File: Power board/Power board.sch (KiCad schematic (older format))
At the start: 6 parts

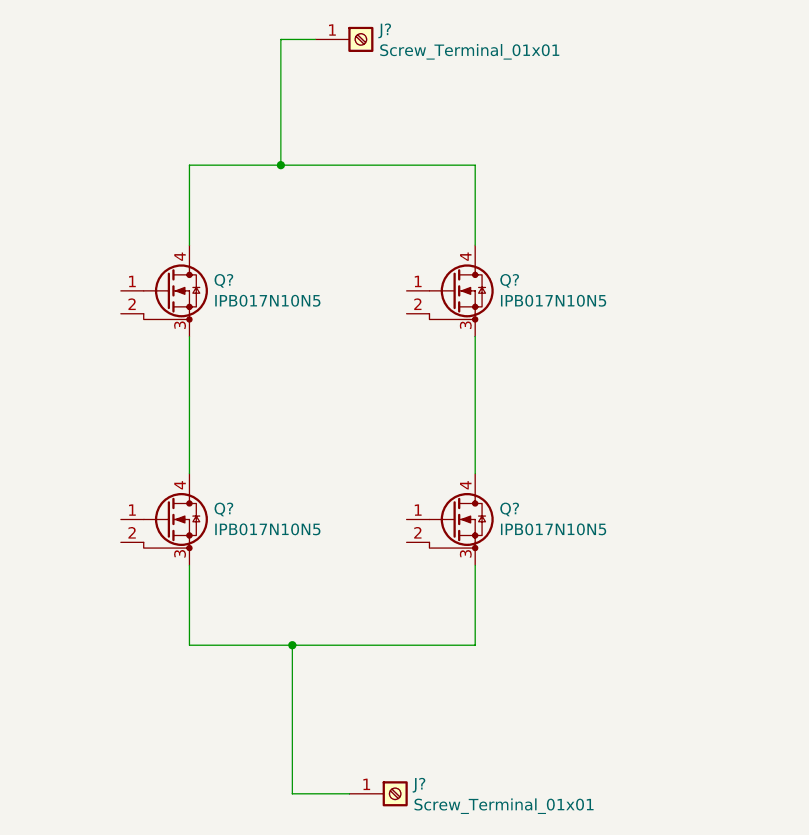
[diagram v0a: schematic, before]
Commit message: Gate resistors is added to power board
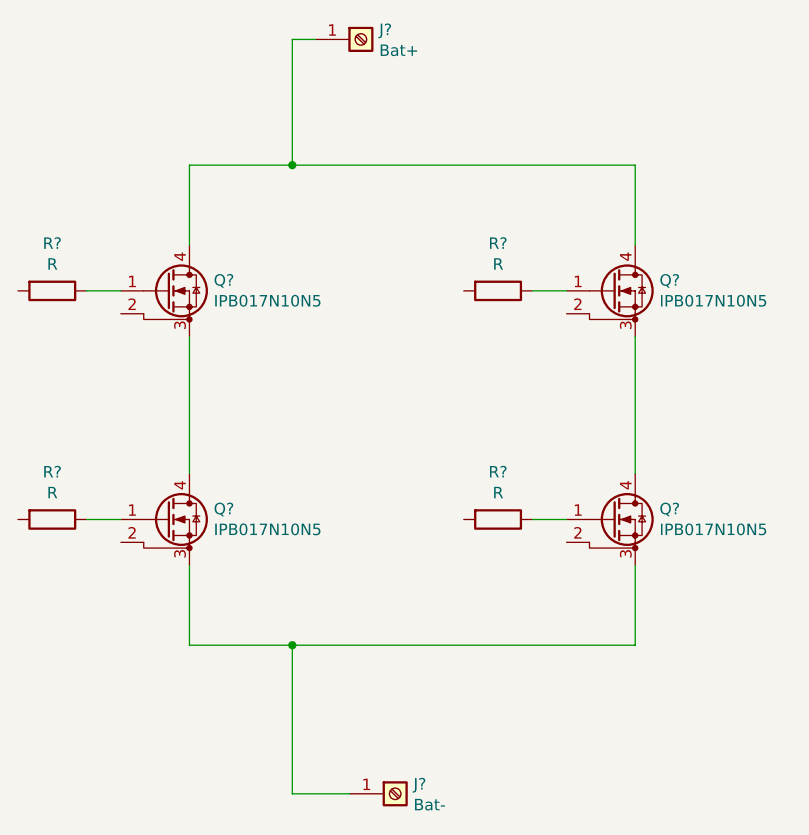
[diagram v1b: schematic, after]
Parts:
- added R? (x4): R, symbol Device:R
- J?: value Screw_Terminal_01x01 -> Bat+
- J?: value Screw_Terminal_01x01 -> Bat-
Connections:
- net at Q?.1 (G): now also R?.1 (x4)
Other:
- moved on the sheet: Q?
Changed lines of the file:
@@
 EESchema Schematic File Version 4
+LIBS:Power board-cache
 EELAYER 29 0
 EELAYER END
@@
 L Vikings_actives:IPB017N10N5 Q?
 U 1 1 5CB8FD8E
-P 5650 2250
-F 0 "Q?" H 5856 2296 50  0000 L CNN
-F 1 "IPB017N10N5" H 5856 2205 50  0000 L CNN
-F 2 "Package_TO_SOT_SMD:TO-263-7_TabPin8" H 5650 2250 50  0001 C CIN
-F 3 "https://www.wolfspeed.com/media/downloads/145/C3M0065090J.pdf" H 5650 2250 50  0001 L CNN
-	1    5650 2250
+P 6350 2250
+F 0 "Q?" H 6556 2296 50  0000 L CNN
+F 1 "IPB017N10N5" H 6556 2205 50  0000 L CNN
+F 2 "Package_TO_SOT_SMD:TO-263-7_TabPin8" H 6350 2250 50  0001 C CIN
+F 3 "https://www.wolfspeed.com/media/downloads/145/C3M0065090J.pdf" H 6350 2250 50  0001 L CNN
+	1    6350 2250
 	1    0    0    -1
 $EndComp
@@
 L Vikings_actives:IPB017N10N5 Q?
 U 1 1 5CB94E76
-P 5650 3250
-F 0 "Q?" H 5856 3296 50  0000 L CNN
-F 1 "IPB017N10N5" H 5856 3205 50  0000 L CNN
-F 2 "Package_TO_SOT_SMD:TO-263-7_TabPin8" H 5650 3250 50  0001 C CIN
-F 3 "https://www.wolfspeed.com/media/downloads/145/C3M0065090J.pdf" H 5650 3250 50  0001 L CNN
-	1    5650 3250
+P 6350 3250
+F 0 "Q?" H 6556 3296 50  0000 L CNN
+F 1 "IPB017N10N5" H 6556 3205 50  0000 L CNN
+F 2 "Package_TO_SOT_SMD:TO-263-7_TabPin8" H 6350 3250 50  0001 C CIN
+F 3 "https://www.wolfspeed.com/media/downloads/145/C3M0065090J.pdf" H 6350 3250 50  0001 L CNN
+	1    6350 3250
 	1    0    0    -1
 $EndComp
@@
 P 5250 1150
 F 0 "J?" H 5330 1192 50  0000 L CNN
-F 1 "Screw_Terminal_01x01" H 5330 1101 50  0000 L CNN
+F 1 "Bat+" H 5330 1101 50  0000 L CNN
 F 2 "" H 5250 1150 50  0001 C CNN
 F 3 "~" H 5250 1150 50  0001 C CNN
@@
 $EndComp
 Wire Wire Line
-	5050 1150 4900 1150
-Wire Wire Line
-	4900 1150 4900 1700
-Wire Wire Line
-	4900 1700 4500 1700
-Wire Wire Line
 	4500 1700 4500 2050
 Wire Wire Line
-	4900 1700 5750 1700
-Wire Wire Line
-	5750 1700 5750 2050
-Connection ~ 4900 1700
+	6450 1700 6450 2050
 Wire Wire Line
 	4500 2450 4500 3050
 Wire Wire Line
-	5750 2450 5750 3050
+	6450 2450 6450 3050
 Wire Wire Line
-	5750 3450 5750 3800
-Wire Wire Line
-	5750 3800 4950 3800
+	6450 3450 6450 3800
 Wire Wire Line
 	4500 3800 4500 3450
@@
 P 5400 4450
 F 0 "J?" H 5480 4492 50  0000 L CNN
-F 1 "Screw_Terminal_01x01" H 5480 4401 50  0000 L CNN
+F 1 "Bat-" H 5480 4401 50  0000 L CNN
 F 2 "" H 5400 4450 50  0001 C CNN
 F 3 "~" H 5400 4450 50  0001 C CNN
@@
 Wire Wire Line
 	4950 4450 4950 3800
-Connection ~ 4950 3800
 Wire Wire Line
 	4950 3800 4500 3800
+$Comp
+L Device:R R?
+U 1 1 5CC099DA
+P 3900 2250
+F 0 "R?" V 3693 2250 50  0000 C CNN
+F 1 "R" V 3784 2250 50  0000 C CNN
+F 2 "" V 3830 2250 50  0001 C CNN
+F 3 "~" H 3900 2250 50  0001 C CNN
+	1    3900 2250
+	0    1    1    0
+$EndComp
+$Comp
+L Device:R R?
+U 1 1 5CC0B578
+P 3900 3250
+F 0 "R?" V 3693 3250 50  0000 C CNN
+F 1 "R" V 3784 3250 50  0000 C CNN
+F 2 "" V 3830 3250 50  0001 C CNN
+F 3 "~" H 3900 3250 50  0001 C CNN
+	1    3900 3250
+	0    1    1    0
+$EndComp
+$Comp
+L Device:R R?
+U 1 1 5CC0C047
+P 5850 3250
+F 0 "R?" V 5643 3250 50  0000 C CNN
+F 1 "R" V 5734 3250 50  0000 C CNN
+F 2 "" V 5780 3250 50  0001 C CNN
+F 3 "~" H 5850 3250 50  0001 C CNN
+	1    5850 3250
+	0    1    1    0
+$EndComp
+Wire Wire Line
+	4950 3800 6450 3800
+Connection ~ 4950 3800
+$Comp
+L Device:R R?
+U 1 1 5CC100FA
+P 5850 2250
+F 0 "R?" V 5643 2250 50  0000 C CNN
+F 1 "R" V 5734 2250 50  0000 C CNN
+F 2 "" V 5780 2250 50  0001 C CNN
+F 3 "~" H 5850 2250 50  0001 C CNN
+	1    5850 2250
+	0    1    1    0
+$EndComp
+Wire Wire Line
+	4500 1700 4950 1700
+Wire Wire Line
+	4950 1700 4950 1150
+Wire Wire Line
+	4950 1150 5050 1150
+Connection ~ 4950 1700
+Wire Wire Line
+	4950 1700 6450 1700
+Wire Wire Line
+	6150 2250 6000 2250
+Wire Wire Line
+	4200 2250 4050 2250
+Wire Wire Line
+	6150 3250 6000 3250
+Wire Wire Line
+	4200 3250 4050 3250
 $EndSCHEMATC

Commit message: schematic is done
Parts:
- removed J?: Bat+, symbol Connector:Screw_Terminal_01x01
- removed J?: Bat-, symbol Connector:Screw_Terminal_01x01
- added C1, C2: 0.033u, Capacitors_SMD:C_0805, symbol Device:C
- added C3: 1u, Capacitors_SMD:C_0805, symbol Device:C
- added J1: High1, Pin_Headers:Pin_Header_Straight_1x02_Pitch2.54mm_SMD_Pin1Left, symbol Connector_Generic:Conn_01x02
- added J2: Low1, Pin_Headers:Pin_Header_Straight_1x02_Pitch2.54mm_SMD_Pin1Left, symbol Connector_Generic:Conn_01x02
- added J3: High2, Pin_Headers:Pin_Header_Straight_1x02_Pitch2.54mm_SMD_Pin1Left, symbol Connector_Generic:Conn_01x02
- added J4: Low2, Pin_Headers:Pin_Header_Straight_1x02_Pitch2.54mm_SMD_Pin1Left, symbol Connector_Generic:Conn_01x02
- added J5: Bat+, Vikings_misc:Busbar_connection, symbol Connector_Generic:Conn_01x01
- added J6: Bat-, Vikings_misc:Busbar_connection, symbol Connector_Generic:Conn_01x01
- added J7: Phase, Vikings_connectors:Würth_PowerOne_SMD_M8, symbol Connector:Screw_Terminal_01x01
- added R5, R6: 1, Resistors_SMD:R_0805, symbol Device:R
- R1, R2, R3, R4: renamed from R?; value R -> 4.7; footprint (none) -> Resistors_SMD:R_0805
- gave numbers to parts that had none: 4
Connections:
- net at Q1.2 (DS): now also J1.1 (Pin_1)
- net at Q1.3 (S), Q1.5 (S), Q1.6 (S)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: now also Q3.3 (S), Q3.5 (S), Q3.6 (S), Q3.7 (S), Q4.4 (D), J7.1 (Pin_1), R5.2, R6.1
- net at Q1.4 (D), Q3.4 (D): now also C1.1, C3.1, J5.1 (Pin_1)
- net at Q3.2 (DS): now also J3.1 (Pin_1)
- net at Q2.2 (DS): now also J2.1 (Pin_1)
- net at Q2.3 (S), Q2.5 (S), Q2.6 (S)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: now also C2.2, C3.2, J6.1 (Pin_1)
- net at Q4.2 (DS): now also J4.1 (Pin_1)
- net at R1.2: now also J1.2 (Pin_2)
- net at R2.2: now also J2.2 (Pin_2)
- net at R4.2: now also J4.2 (Pin_2)
- net at R3.2: now also J3.2 (Pin_2)
- new net: C1.2, R5.1
- new net: C2.1, R6.2

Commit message: Power board is done
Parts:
- added C5: 1u, Capacitors_SMD:C_2220, symbol Device:C
- added C6, C7: 1u, Capacitors_SMD:C_0805, symbol Device:C
- added J10: 2x2_pin_bat+, Pin_Headers:Pin_Header_Straight_2x02_Pitch2.54mm_SMD, symbol Connector_Generic:Conn_02x02_Counter_Clockwise
- added J11: 2x2_pin_bat-, Pin_Headers:Pin_Header_Straight_2x02_Pitch2.54mm_SMD, symbol Connector_Generic:Conn_02x02_Counter_Clockwise
- added J8: 2x2_pin_support1, Pin_Headers:Pin_Header_Straight_2x02_Pitch2.54mm_SMD, symbol Connector_Generic:Conn_02x02_Counter_Clockwise
- added J9: 2x2_pin_support2, Pin_Headers:Pin_Header_Straight_2x02_Pitch2.54mm_SMD, symbol Connector_Generic:Conn_02x02_Counter_Clockwise
- Q1, Q2, Q3, Q4: footprint Package_TO_SOT_SMD:TO-263-7_TabPin8 -> TO_SOT_Packages_SMD:TO-263-7_TabPin4
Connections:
- net Bat+: now reaches C1.1, C3.1, J5.1 (Pin_1), Q1.4 (D), Q3.4 (D)
- net Bat+: now also C5.1, C6.1, C7.1, J10.1 (Pin_1), J10.2 (Pin_2), J10.3 (Pin_3), J10.4 (Pin_4)
- net Bat-: now reaches C2.2, C3.2, J6.1 (Pin_1), Q2.3 (S), Q2.5 (S), Q2.6 (S), Q2.7 (S), Q4.3 (S), Q4.5 (S), Q4.6 (S), Q4.7 (S)
- net Bat-: now also C5.2, C6.2, C7.2, J11.1 (Pin_1), J11.2 (Pin_2), J11.3 (Pin_3), J11.4 (Pin_4)
- no-connect marks 0 -> 8
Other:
- moved on the sheet: J5, J6
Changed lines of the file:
@@
 F 0 "Q1" H 4606 2296 50  0000 L CNN
 F 1 "IPB017N10N5" H 4606 2205 50  0000 L CNN
-F 2 "Package_TO_SOT_SMD:TO-263-7_TabPin8" H 4400 2250 50  0001 C CIN
+F 2 "TO_SOT_Packages_SMD:TO-263-7_TabPin4" H 4400 2250 50  0001 C CIN
 F 3 "https://www.wolfspeed.com/media/downloads/145/C3M0065090J.pdf" H 4400 2250 50  0001 L CNN
 	1    4400 2250
@@
 F 0 "Q3" H 6556 2296 50  0000 L CNN
 F 1 "IPB017N10N5" H 6556 2205 50  0000 L CNN
-F 2 "Package_TO_SOT_SMD:TO-263-7_TabPin8" H 6350 2250 50  0001 C CIN
+F 2 "TO_SOT_Packages_SMD:TO-263-7_TabPin4" H 6350 2250 50  0001 C CIN
 F 3 "https://www.wolfspeed.com/media/downloads/145/C3M0065090J.pdf" H 6350 2250 50  0001 L CNN
 	1    6350 2250
@@
 F 0 "Q2" H 4606 3296 50  0000 L CNN
 F 1 "IPB017N10N5" H 4606 3205 50  0000 L CNN
-F 2 "Package_TO_SOT_SMD:TO-263-7_TabPin8" H 4400 3250 50  0001 C CIN
+F 2 "TO_SOT_Packages_SMD:TO-263-7_TabPin4" H 4400 3250 50  0001 C CIN
 F 3 "https://www.wolfspeed.com/media/downloads/145/C3M0065090J.pdf" H 4400 3250 50  0001 L CNN
 	1    4400 3250
@@
 F 0 "Q4" H 6556 3296 50  0000 L CNN
 F 1 "IPB017N10N5" H 6556 3205 50  0000 L CNN
-F 2 "Package_TO_SOT_SMD:TO-263-7_TabPin8" H 6350 3250 50  0001 C CIN
+F 2 "TO_SOT_Packages_SMD:TO-263-7_TabPin4" H 6350 3250 50  0001 C CIN
 F 3 "https://www.wolfspeed.com/media/downloads/145/C3M0065090J.pdf" H 6350 3250 50  0001 L CNN
 	1    6350 3250
@@
 L Connector_Generic:Conn_01x01 J5
 U 1 1 5CC301E6
-P 2550 1700
-F 0 "J5" H 2468 1475 50  0000 C CNN
-F 1 "Bat+" H 2468 1566 50  0000 C CNN
-F 2 "Vikings_misc:Busbar_connection" H 2550 1700 50  0001 C CNN
-F 3 "~" H 2550 1700 50  0001 C CNN
-	1    2550 1700
+P 800 1700
+F 0 "J5" H 718 1475 50  0000 C CNN
+F 1 "Bat+" H 718 1566 50  0000 C CNN
+F 2 "Vikings_misc:Busbar_connection" H 800 1700 50  0001 C CNN
+F 3 "~" H 800 1700 50  0001 C CNN
+	1    800  1700
 	-1   0    0    1
 $EndComp
@@
 L Connector_Generic:Conn_01x01 J6
 U 1 1 5CC30934
-P 2550 3800
-F 0 "J6" H 2468 3575 50  0000 C CNN
-F 1 "Bat-" H 2468 3666 50  0000 C CNN
-F 2 "Vikings_misc:Busbar_connection" H 2550 3800 50  0001 C CNN
-F 3 "~" H 2550 3800 50  0001 C CNN
-	1    2550 3800
-	-1   0    0    1
-$EndComp
-Wire Wire Line
-	2750 1700 3100 1700
+P 800 3800
+F 0 "J6" H 718 3575 50  0000 C CNN
+F 1 "Bat-" H 718 3666 50  0000 C CNN
+F 2 "Vikings_misc:Busbar_connection" H 800 3800 50  0001 C CNN
+F 3 "~" H 800 3800 50  0001 C CNN
+	1    800  3800
+	-1   0    0    1
+$EndComp
 Connection ~ 4500 1700
 Connection ~ 4500 3800
 Wire Wire Line
 	3100 2600 3100 1700
-Connection ~ 3100 1700
 Wire Wire Line
 	3100 1700 4500 1700
 Wire Wire Line
 	3100 2900 3100 3800
-Connection ~ 3100 3800
-Wire Wire Line
-	3100 3800 2750 3800
 Wire Wire Line
 	4500 3800 3100 3800
@@
 Wire Wire Line
 	6450 1700 7350 1700
+$Comp
+L Connector_Generic:Conn_02x02_Counter_Clockwise J9
+U 1 1 5CC51E4B
+P 7250 850
+F 0 "J9" H 7300 1067 50  0000 C CNN
+F 1 "2x2_pin_support2" H 7300 976 50  0000 C CNN
+F 2 "Pin_Headers:Pin_Header_Straight_2x02_Pitch2.54mm_SMD" H 7250 850 50  0001 C CNN
+F 3 "~" H 7250 850 50  0001 C CNN
+	1    7250 850
+	1    0    0    -1
+$EndComp
+$Comp
+L Connector_Generic:Conn_02x02_Counter_Clockwise J10
+U 1 1 5CC52F01
+P 9650 1400
+F 0 "J10" H 9700 1617 50  0000 C CNN
+F 1 "2x2_pin_bat+" H 9700 1526 50  0000 C CNN
+F 2 "Pin_Headers:Pin_Header_Straight_2x02_Pitch2.54mm_SMD" H 9650 1400 50  0001 C CNN
+F 3 "~" H 9650 1400 50  0001 C CNN
+	1    9650 1400
+	1    0    0    -1
+$EndComp
+$Comp
+L Connector_Generic:Conn_02x02_Counter_Clockwise J11
+U 1 1 5CC53293
+P 9650 2100
+F 0 "J11" H 9700 2317 50  0000 C CNN
+F 1 "2x2_pin_bat-" H 9700 2226 50  0000 C CNN
+F 2 "Pin_Headers:Pin_Header_Straight_2x02_Pitch2.54mm_SMD" H 9650 2100 50  0001 C CNN
+F 3 "~" H 9650 2100 50  0001 C CNN
+	1    9650 2100
+	1    0    0    -1
+$EndComp
+NoConn ~ 7550 850
+NoConn ~ 7550 950
+NoConn ~ 7050 950
+NoConn ~ 7050 850
+NoConn ~ 6250 850
+NoConn ~ 6250 950
+NoConn ~ 5750 850
+Text Label 1100 1700 0    50   ~ 0
+Bat+
+Text Label 1050 3800 0    50   ~ 0
+Bat-
+Wire Wire Line
+	9450 1400 9400 1400
+Wire Wire Line
+	9400 1400 9400 1500
+Wire Wire Line
+	9400 1500 9450 1500
+Wire Wire Line
+	9950 1400 10050 1400
+Wire Wire Line
+	10050 1400 10050 1500
+Wire Wire Line
+	10050 1500 9950 1500
+Wire Wire Line
+	10050 1500 10050 1650
+Wire Wire Line
+	10050 1650 9400 1650
+Wire Wire Line
+	9400 1650 9400 1500
+Connection ~ 10050 1500
+Connection ~ 9400 1500
+Text Label 9150 1650 0    50   ~ 0
+Bat+
+Wire Wire Line
+	9400 1650 9150 1650
+Connection ~ 9400 1650
+Wire Wire Line
+	9450 2100 9400 2100
+Wire Wire Line
+	9400 2100 9400 2200
+Wire Wire Line
+	9400 2200 9450 2200
+Wire Wire Line
+	9950 2100 10050 2100
+Wire Wire Line
+	10050 2100 10050 2200
+Wire Wire Line
+	10050 2200 9950 2200
+Wire Wire Line
+	10050 2200 10050 2350
+Wire Wire Line
+	10050 2350 9400 2350
+Wire Wire Line
+	9400 2350 9400 2200
+Connection ~ 10050 2200
+Connection ~ 9400 2200
+Text Label 9150 2350 0    50   ~ 0
+Bat-
+Wire Wire Line
+	9150 2350 9400 2350
+Connection ~ 9400 2350
+NoConn ~ 5750 950
+$Comp
+L Connector_Generic:Conn_02x02_Counter_Clockwise J8
+U 1 1 5CC537D4
+P 5950 850
+F 0 "J8" H 6000 1067 50  0000 C CNN
+F 1 "2x2_pin_support1" H 6000 976 50  0000 C CNN
+F 2 "Pin_Headers:Pin_Header_Straight_2x02_Pitch2.54mm_SMD" H 5950 850 50  0001 C CNN
+F 3 "~" H 5950 850 50  0001 C CNN
+	1    5950 850
+	1    0    0    -1
+$EndComp
+$Comp
+L Device:C C7
+U 1 1 5CC97E3D
+P 2700 2750
+F 0 "C7" H 2815 2796 50  0000 L CNN
+F 1 "1u" H 2815 2705 50  0000 L CNN
+F 2 "Capacitors_SMD:C_0805" H 2738 2600 50  0001 C CNN
+F 3 "~" H 2700 2750 50  0001 C CNN
+	1    2700 2750
+	1    0    0    -1
+$EndComp
+$Comp
+L Device:C C6
+U 1 1 5CC98333
+P 2350 2750
+F 0 "C6" H 2465 2796 50  0000 L CNN
+F 1 "1u" H 2465 2705 50  0000 L CNN
+F 2 "Capacitors_SMD:C_0805" H 2388 2600 50  0001 C CNN
+F 3 "~" H 2350 2750 50  0001 C CNN
+	1    2350 2750
+	1    0    0    -1
+$EndComp
+$Comp
+L Device:C C5
+U 1 1 5CC9876E
+P 2000 2750
+F 0 "C5" H 2115 2796 50  0000 L CNN
+F 1 "1u" H 2115 2705 50  0000 L CNN
+F 2 "Capacitors_SMD:C_2220" H 2038 2600 50  0001 C CNN
+F 3 "~" H 2000 2750 50  0001 C CNN
+	1    2000 2750
+	1    0    0    -1
+$EndComp
+Connection ~ 3100 1700
+Connection ~ 3100 3800
+Wire Wire Line
+	2000 2900 2000 3800
+Connection ~ 2000 3800
+Wire Wire Line
+	2000 3800 2350 3800
+Wire Wire Line
+	2350 2900 2350 3800
+Connection ~ 2350 3800
+Wire Wire Line
+	2350 3800 2700 3800
+Wire Wire Line
+	2700 2900 2700 3800
+Connection ~ 2700 3800
+Wire Wire Line
+	2700 3800 3100 3800
+Wire Wire Line
+	2700 2600 2700 1700
+Connection ~ 2700 1700
+Wire Wire Line
+	2700 1700 3100 1700
+Wire Wire Line
+	2350 2600 2350 1700
+Connection ~ 2350 1700
+Wire Wire Line
+	2350 1700 2700 1700
+Wire Wire Line
+	2000 2600 2000 1700
+Connection ~ 2000 1700
+Wire Wire Line
+	2000 1700 2350 1700
+Wire Wire Line
+	1000 1700 2000 1700
+Wire Wire Line
+	1000 3800 2000 3800
 $EndSCHEMATC

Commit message: Done PCB
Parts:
- added C4: C, Capacitors_SMD:C_0805, symbol Device:C
- added C8: C, Capacitors_SMD:C_2220, symbol Device:C
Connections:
- net Bat+: now also C4.1, C8.1
- net Bat-: now also C4.2, C8.2
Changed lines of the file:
@@
 	2000 1700 2350 1700
 Wire Wire Line
-	1000 1700 2000 1700
+	1000 1700 1350 1700
 Wire Wire Line
-	1000 3800 2000 3800
+	1000 3800 1350 3800
+$Comp
+L Device:C C8
+U 1 1 5CC2C8AA
+P 1600 2750
+F 0 "C8" H 1715 2796 50  0000 L CNN
+F 1 "C" H 1715 2705 50  0000 L CNN
+F 2 "Capacitors_SMD:C_2220" H 1638 2600 50  0001 C CNN
+F 3 "~" H 1600 2750 50  0001 C CNN
+	1    1600 2750
+	1    0    0    -1
+$EndComp
+$Comp
+L Device:C C4
+U 1 1 5CC2CCD9
+P 1350 2750
+F 0 "C4" H 1465 2796 50  0000 L CNN
+F 1 "C" H 1465 2705 50  0000 L CNN
+F 2 "Capacitors_SMD:C_0805" H 1388 2600 50  0001 C CNN
+F 3 "~" H 1350 2750 50  0001 C CNN
+	1    1350 2750
+	1    0    0    -1
+$EndComp
+Wire Wire Line
+	1600 2600 1600 1700
+Connection ~ 1600 1700
+Wire Wire Line
+	1600 1700 2000 1700
+Wire Wire Line
+	1350 2600 1350 1700
+Connection ~ 1350 1700
+Wire Wire Line
+	1350 1700 1600 1700
+Wire Wire Line
+	1350 2900 1350 3800
+Connection ~ 1350 3800
+Wire Wire Line
+	1350 3800 1600 3800
+Wire Wire Line
+	1600 2900 1600 3800
+Connection ~ 1600 3800
+Wire Wire Line
+	1600 3800 2000 3800
 $EndSCHEMATC
